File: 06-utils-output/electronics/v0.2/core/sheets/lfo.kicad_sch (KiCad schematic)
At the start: 15 parts, among them Q4 BC848, U3 TL072

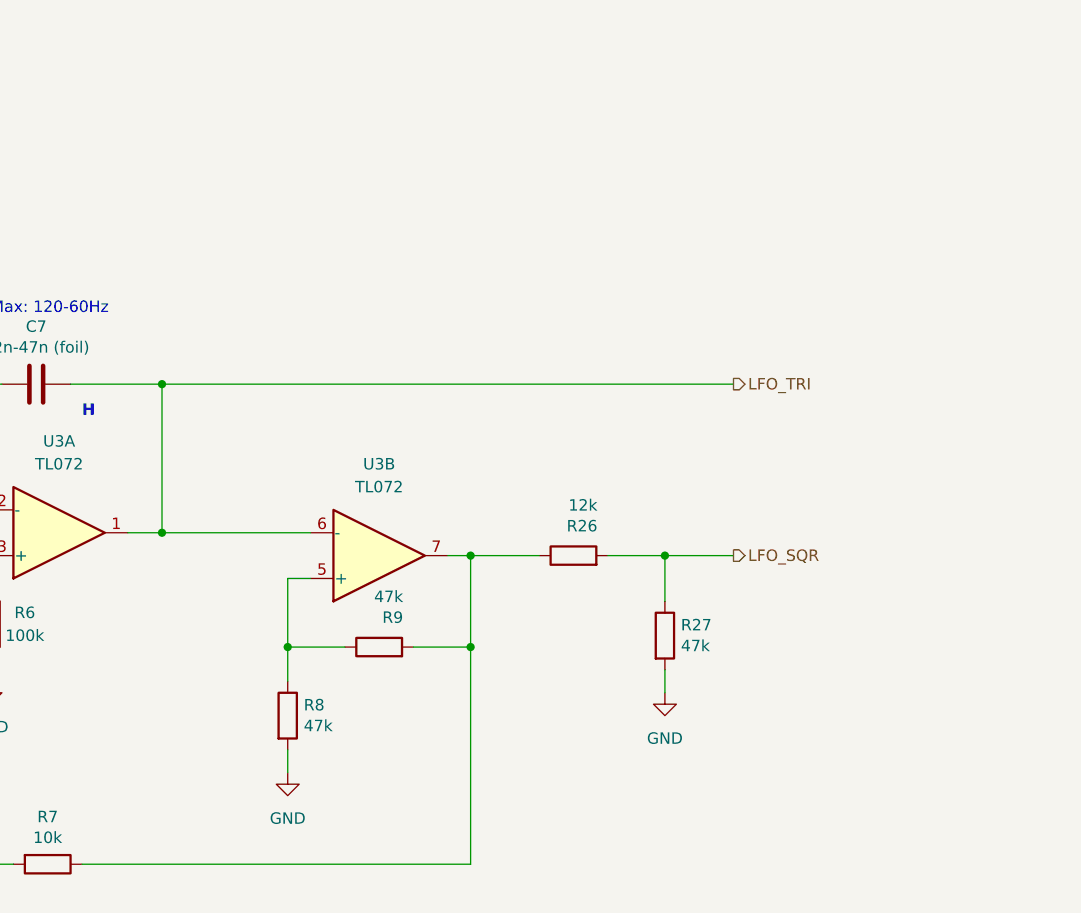
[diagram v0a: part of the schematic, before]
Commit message: Added protection diodes to utils + output
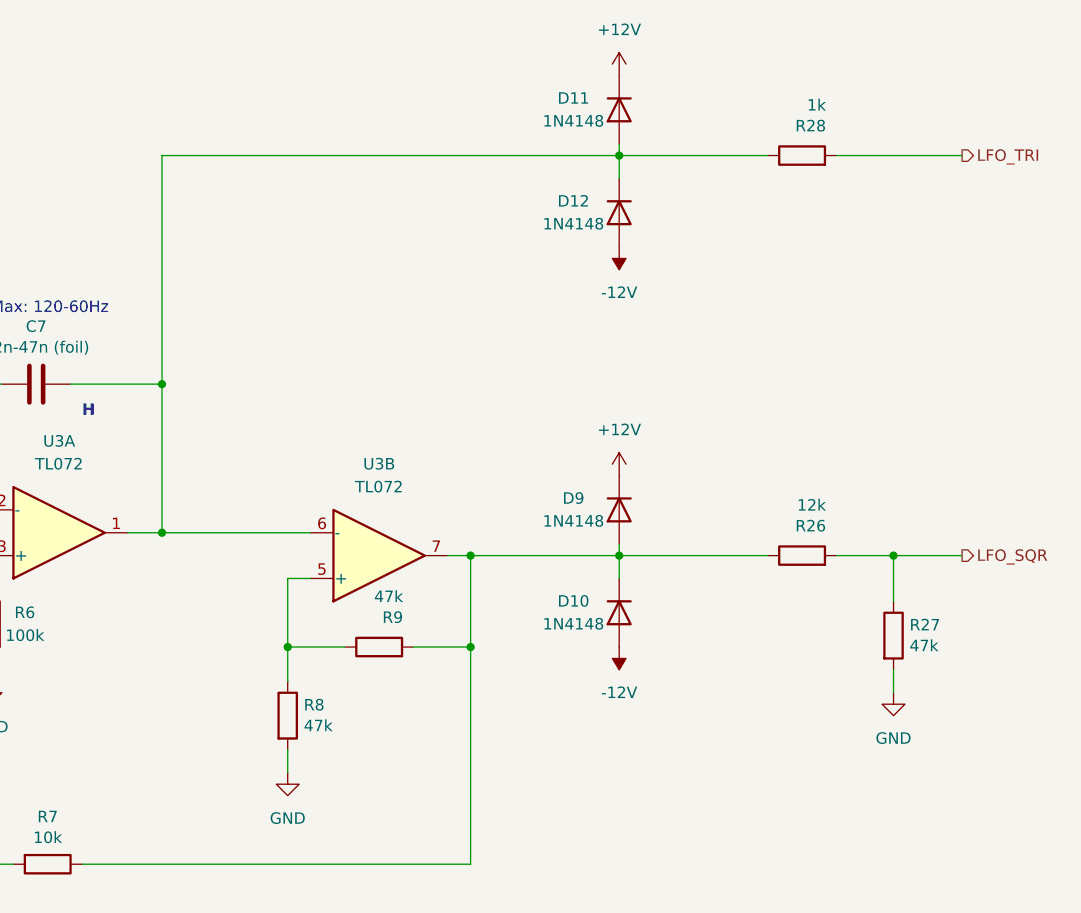
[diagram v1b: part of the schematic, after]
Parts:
- added D10, D11, D12, D9: 1N4148, Diode_SMD:D_SOD-123, symbol Device:D
- added R28: 1k, Resistor_SMD:R_0603_1608Metric, symbol Device:R
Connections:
- net +12V: now also D11.1 (K), D9.1 (K)
- net -12V: now also D10.2 (A), D12.2 (A)
- net LFO_TRI: now also R28.2; no longer C7.1, U3.1, U3.6 (-)
- net at R26.1, R7.1, R9.2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: now also D10.1 (K), D9.2 (A)
- new net: C7.1, D11.2 (A), D12.1 (K), R28.1, U3.1, U3.6 (-)
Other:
- moved on the sheet: R26, R27

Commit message: Bitcrusher tested and  refined
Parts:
- renumbered D10 to #D10, D11 to #D11, D12 to #D12, D9 to #D9
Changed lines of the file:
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@@
 		(on_board yes)
 		(dnp no)
-		(property "Reference" "D11"
+		(property "Reference" "#D11"
 			(at 205.74 36.83 90)
 			(effects
@@
 			(project "utils-output-core"
 				(path "/8e2e31f3-eed5-4de1-966c-f4162758c735/0d9d761e-1d4a-435a-b5d8-d58fdf2908d4"
-					(reference "D11")
+					(reference "#D11")
 					(unit 1)
 				)
@@
 		(on_board yes)
 		(dnp no)
-		(property "Reference" "D10"
+		(property "Reference" "#D10"
 			(at 205.74 92.71 90)
 			(effects
@@
 			(project "utils-output-core"
 				(path "/8e2e31f3-eed5-4de1-966c-f4162758c735/0d9d761e-1d4a-435a-b5d8-d58fdf2908d4"
-					(reference "D10")
+					(reference "#D10")
 					(unit 1)
 				)
@@
 		(on_board yes)
 		(dnp no)
-		(property "Reference" "D9"
+		(property "Reference" "#D9"
 			(at 205.74 81.28 90)
 			(effects
@@
 			(project "utils-output-core"
 				(path "/8e2e31f3-eed5-4de1-966c-f4162758c735/0d9d761e-1d4a-435a-b5d8-d58fdf2908d4"
-					(reference "D9")
+					(reference "#D9")
 					(unit 1)
 				)
@@
 		(on_board yes)
 		(dnp no)
-		(property "Reference" "D12"
+		(property "Reference" "#D12"
 			(at 205.74 48.26 90)
 			(effects
@@
 			(project "utils-output-core"
 				(path "/8e2e31f3-eed5-4de1-966c-f4162758c735/0d9d761e-1d4a-435a-b5d8-d58fdf2908d4"
-					(reference "D12")
+					(reference "#D12")
 					(unit 1)
 				)
